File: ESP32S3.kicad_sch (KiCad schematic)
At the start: 7 parts, among them U2 ESP32-S3-WROOM-1

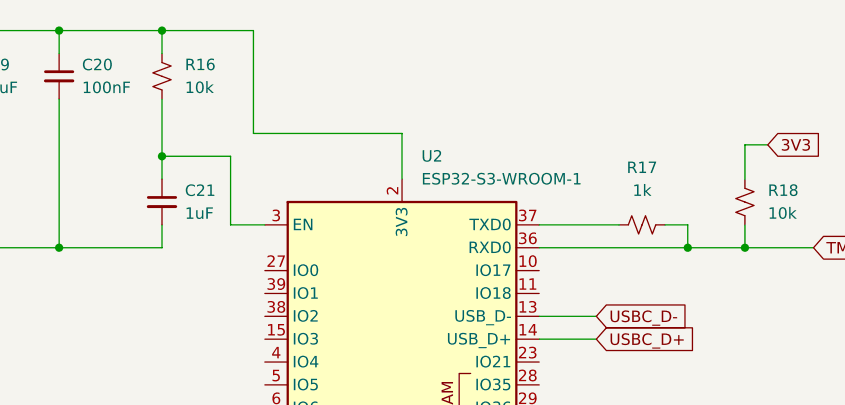
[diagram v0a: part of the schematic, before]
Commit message: updated components and nets
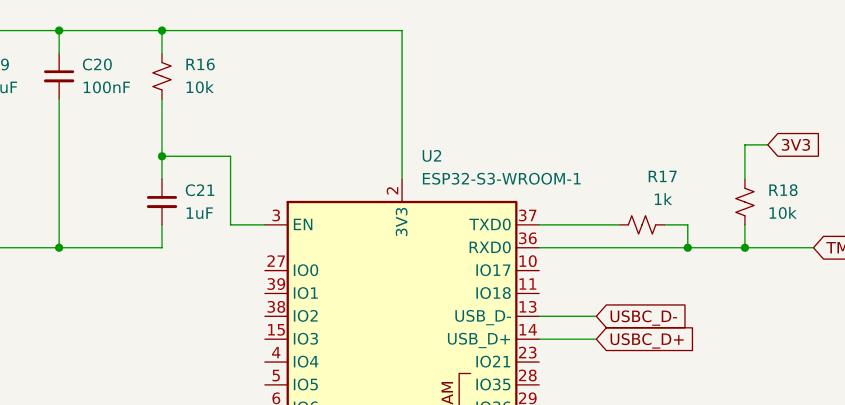
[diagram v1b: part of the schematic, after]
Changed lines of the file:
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@@
-	(wire
-		(pts
-			(xy 130.81 73.66) (xy 147.32 73.66)
-		)
-		(stroke
-			(width 0)
-			(type default)
-		)
-	)
 	(wire
 		(pts
@@
 	(wire
 		(pts
-			(xy 120.65 62.23) (xy 130.81 62.23)
+			(xy 120.65 62.23) (xy 147.32 62.23)
 		)
 		(stroke
@@
 	(wire
 		(pts
-			(xy 147.32 73.66) (xy 147.32 78.74)
+			(xy 147.32 62.23) (xy 147.32 78.74)
 		)
 		(stroke
@@
 		(pts
 			(xy 120.65 76.2) (xy 128.27 76.2)
-		)
-		(stroke
-			(width 0)
-			(type default)
-		)
-	)
-	(wire
-		(pts
-			(xy 130.81 62.23) (xy 130.81 73.66)
 		)
 		(stroke
@@
 		(on_board yes)
 		(dnp no)
-		(fields_autoplaced yes)
 		(property "Reference" "R17"
-			(at 173.99 77.47 90)
+			(at 176.276 78.486 90)
 			(effects
 				(font
@@
 		)
 		(property "Value" "1k"
-			(at 173.99 80.01 90)
-			(effects
-				(font
+			(at 176.276 81.026 90)
+			(effects
+				(font
